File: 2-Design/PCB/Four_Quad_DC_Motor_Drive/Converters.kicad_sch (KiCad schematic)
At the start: 4 parts

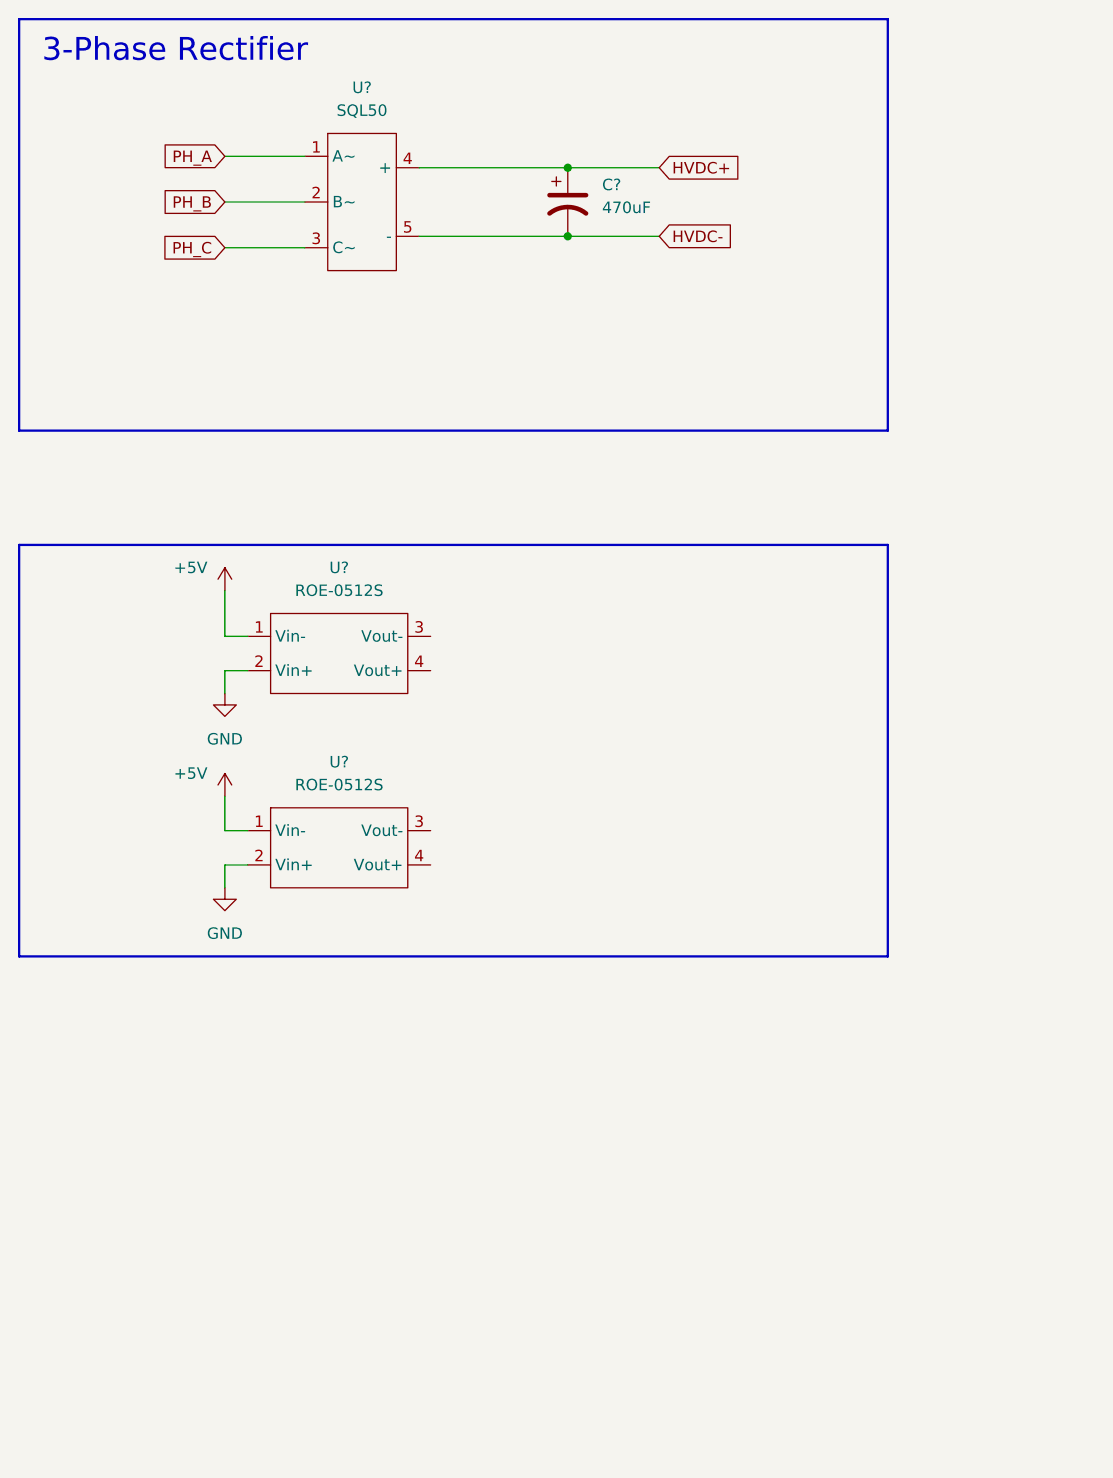
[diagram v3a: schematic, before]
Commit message: Added the gate driver schematics and converter schematics
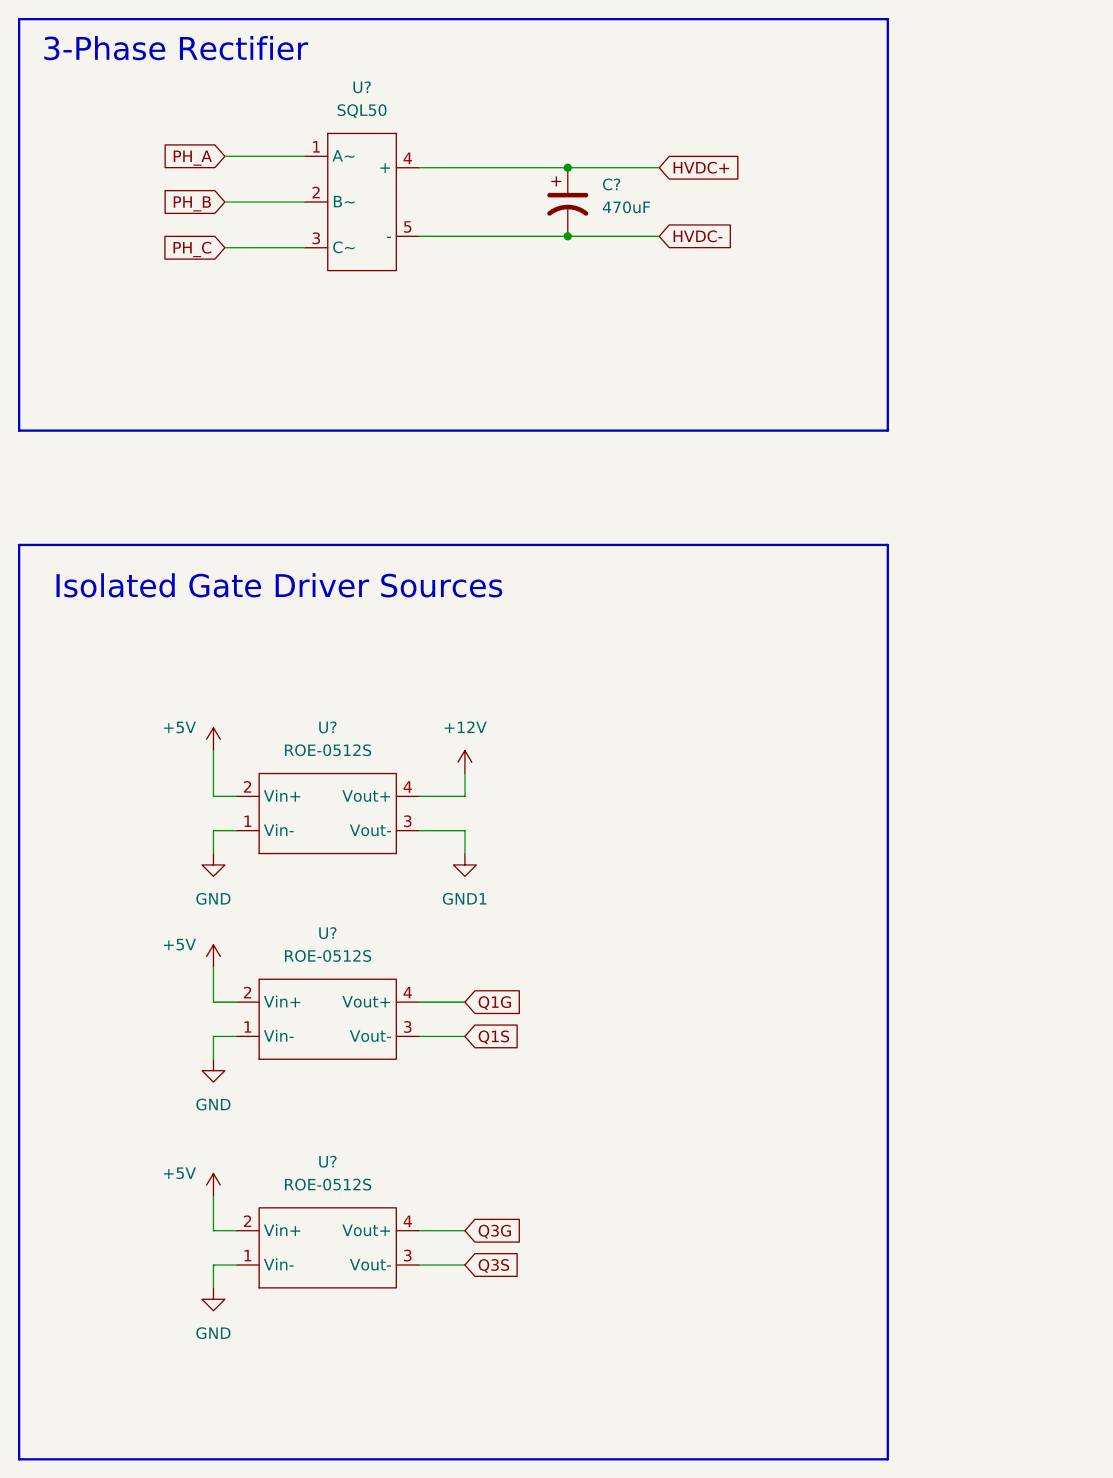
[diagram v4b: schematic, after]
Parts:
- added U?: ROE-0512S, symbol ee463_symbol_library:ROE-0512S
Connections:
- net +5V: now also U?.2 (Vin+), U?.2 (Vin+), U?.2 (Vin+); no longer U?.1 (Vin-), U?.1 (Vin-)
- net GND: now also U?.1 (Vin-), U?.1 (Vin-), U?.1 (Vin-); no longer U?.2 (Vin+), U?.2 (Vin+)
- net Q1S: now reaches U?.3 (Vout-)
- net Q1G: now reaches U?.4 (Vout+)
- net GND1: now reaches U?.3 (Vout-)
- net +12V: now reaches U?.4 (Vout+)
- new net Q3G: U?.4 (Vout+)
- new net Q3S: U?.3 (Vout-)
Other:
- note added: "Isolated Gate Driver Sources"
- moved on the sheet: U?

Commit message: Added the label and gate drive resistances
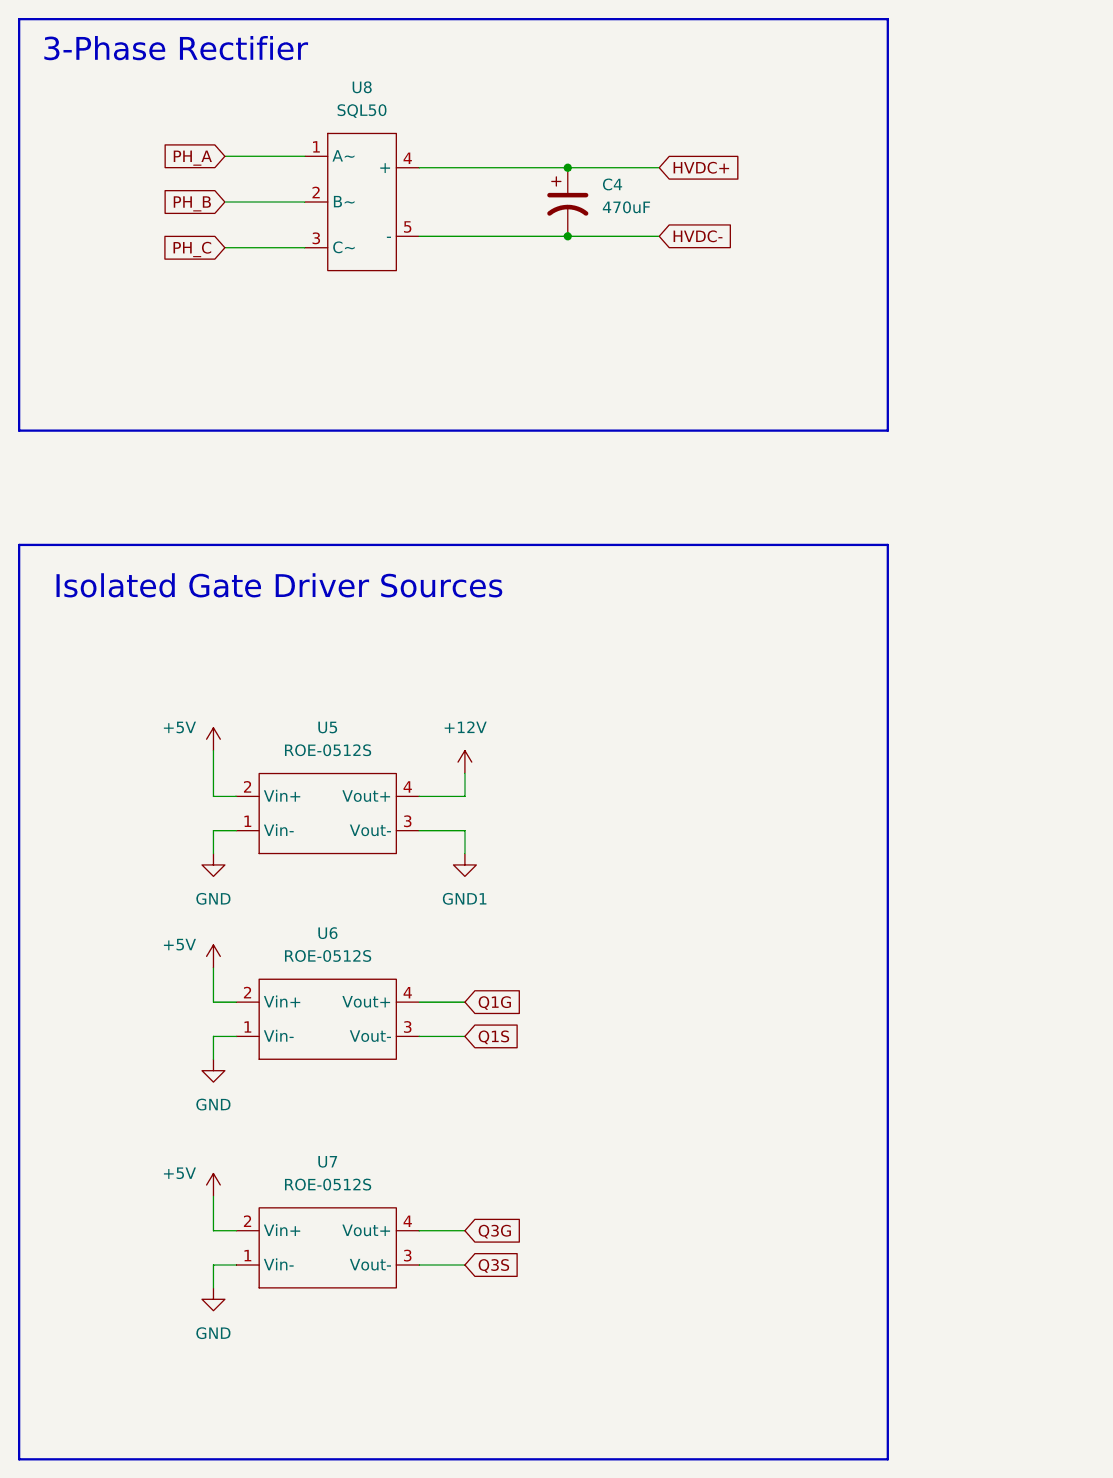
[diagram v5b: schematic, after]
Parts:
- gave numbers to parts that had none: 5
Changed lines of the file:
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@@
   (symbol (lib_id "power:+12V") (at 87.63 104.14 0) (unit 1)
     (in_bom yes) (on_board yes) (fields_autoplaced)
-    (property "Reference" "#PWR?" (id 0) (at 87.63 107.95 0)
+    (property "Reference" "#PWR018" (id 0) (at 87.63 107.95 0)
       (effects (font (size 1.27 1.27)) hide)
     )
@@
   (symbol (lib_id "power:GND") (at 59.69 161.29 0) (unit 1)
     (in_bom yes) (on_board yes) (fields_autoplaced)
-    (property "Reference" "#PWR?" (id 0) (at 59.69 167.64 0)
+    (property "Reference" "#PWR017" (id 0) (at 59.69 167.64 0)
       (effects (font (size 1.27 1.27)) hide)
     )
@@
   (symbol (lib_id "ee463_symbol_library:ROE-0512S") (at 72.39 132.08 0) (mirror x) (unit 1)
     (in_bom yes) (on_board yes) (fields_autoplaced)
-    (property "Reference" "U?" (id 0) (at 72.39 121.92 0))
+    (property "Reference" "U6" (id 0) (at 72.39 121.92 0))
     (property "Value" "ROE-0512S" (id 1) (at 72.39 124.46 0))
     (property "Footprint" "" (id 2) (at 72.39 132.08 0)
@@
   (symbol (lib_id "ee463_symbol_library:ROE-0512S") (at 72.39 109.22 0) (mirror x) (unit 1)
     (in_bom yes) (on_board yes) (fields_autoplaced)
-    (property "Reference" "U?" (id 0) (at 72.39 99.06 0))
+    (property "Reference" "U5" (id 0) (at 72.39 99.06 0))
     (property "Value" "ROE-0512S" (id 1) (at 72.39 101.6 0))
     (property "Footprint" "" (id 2) (at 72.39 109.22 0)
@@
   (symbol (lib_id "power:+5V") (at 59.69 101.6 0) (unit 1)
     (in_bom yes) (on_board yes)
-    (property "Reference" "#PWR?" (id 0) (at 59.69 105.41 0)
+    (property "Reference" "#PWR012" (id 0) (at 59.69 105.41 0)
       (effects (font (size 1.27 1.27)) hide)
     )
@@
   (symbol (lib_id "power:+5V") (at 59.69 151.13 0) (unit 1)
     (in_bom yes) (on_board yes)
-    (property "Reference" "#PWR?" (id 0) (at 59.69 154.94 0)
+    (property "Reference" "#PWR016" (id 0) (at 59.69 154.94 0)
       (effects (font (size 1.27 1.27)) hide)
     )
@@
   (symbol (lib_id "power:GND1") (at 87.63 113.03 0) (unit 1)
     (in_bom yes) (on_board yes) (fields_autoplaced)
-    (property "Reference" "#PWR?" (id 0) (at 87.63 119.38 0)
+    (property "Reference" "#PWR019" (id 0) (at 87.63 119.38 0)
       (effects (font (size 1.27 1.27)) hide)
     )
@@
   (symbol (lib_id "Device:C_Polarized_US") (at 99.06 40.64 0) (unit 1)
     (in_bom yes) (on_board yes) (fields_autoplaced)
-    (property "Reference" "C?" (id 0) (at 102.87 38.7349 0)
+    (property "Reference" "C4" (id 0) (at 102.87 38.7349 0)
       (effects (font (size 1.27 1.27)) (justify left))
     )
@@
   (symbol (lib_id "power:GND") (at 59.69 113.03 0) (unit 1)
     (in_bom yes) (on_board yes) (fields_autoplaced)
-    (property "Reference" "#PWR?" (id 0) (at 59.69 119.38 0)
+    (property "Reference" "#PWR013" (id 0) (at 59.69 119.38 0)
       (effects (font (size 1.27 1.27)) hide)
     )
@@
   (symbol (lib_id "ee463_symbol_library:SQL50") (at 76.2 40.64 0) (unit 1)
     (in_bom yes) (on_board yes) (fields_autoplaced)
-    (property "Reference" "U?" (id 0) (at 76.2 27.94 0))
+    (property "Reference" "U8" (id 0) (at 76.2 27.94 0))
     (property "Value" "SQL50" (id 1) (at 76.2 30.48 0))
     (property "Footprint" "" (id 2) (at 76.2 40.64 0)
@@
   (symbol (lib_id "power:GND") (at 59.69 135.89 0) (unit 1)
     (in_bom yes) (on_board yes) (fields_autoplaced)
-    (property "Reference" "#PWR?" (id 0) (at 59.69 142.24 0)
+    (property "Reference" "#PWR015" (id 0) (at 59.69 142.24 0)
       (effects (font (size 1.27 1.27)) hide)
     )
@@
   (symbol (lib_id "power:+5V") (at 59.69 125.73 0) (unit 1)
     (in_bom yes) (on_board yes)
-    (property "Reference" "#PWR?" (id 0) (at 59.69 129.54 0)
+    (property "Reference" "#PWR014" (id 0) (at 59.69 129.54 0)
       (effects (font (size 1.27 1.27)) hide)
     )
@@
   (symbol (lib_id "ee463_symbol_library:ROE-0512S") (at 72.39 157.48 0) (mirror x) (unit 1)
     (in_bom yes) (on_board yes) (fields_autoplaced)
-    (property "Reference" "U?" (id 0) (at 72.39 147.32 0))
+    (property "Reference" "U7" (id 0) (at 72.39 147.32 0))
     (property "Value" "ROE-0512S" (id 1) (at 72.39 149.86 0))
     (property "Footprint" "" (id 2) (at 72.39 157.48 0)

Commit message: Gate driver changed, plus other rearrangements on the schematics
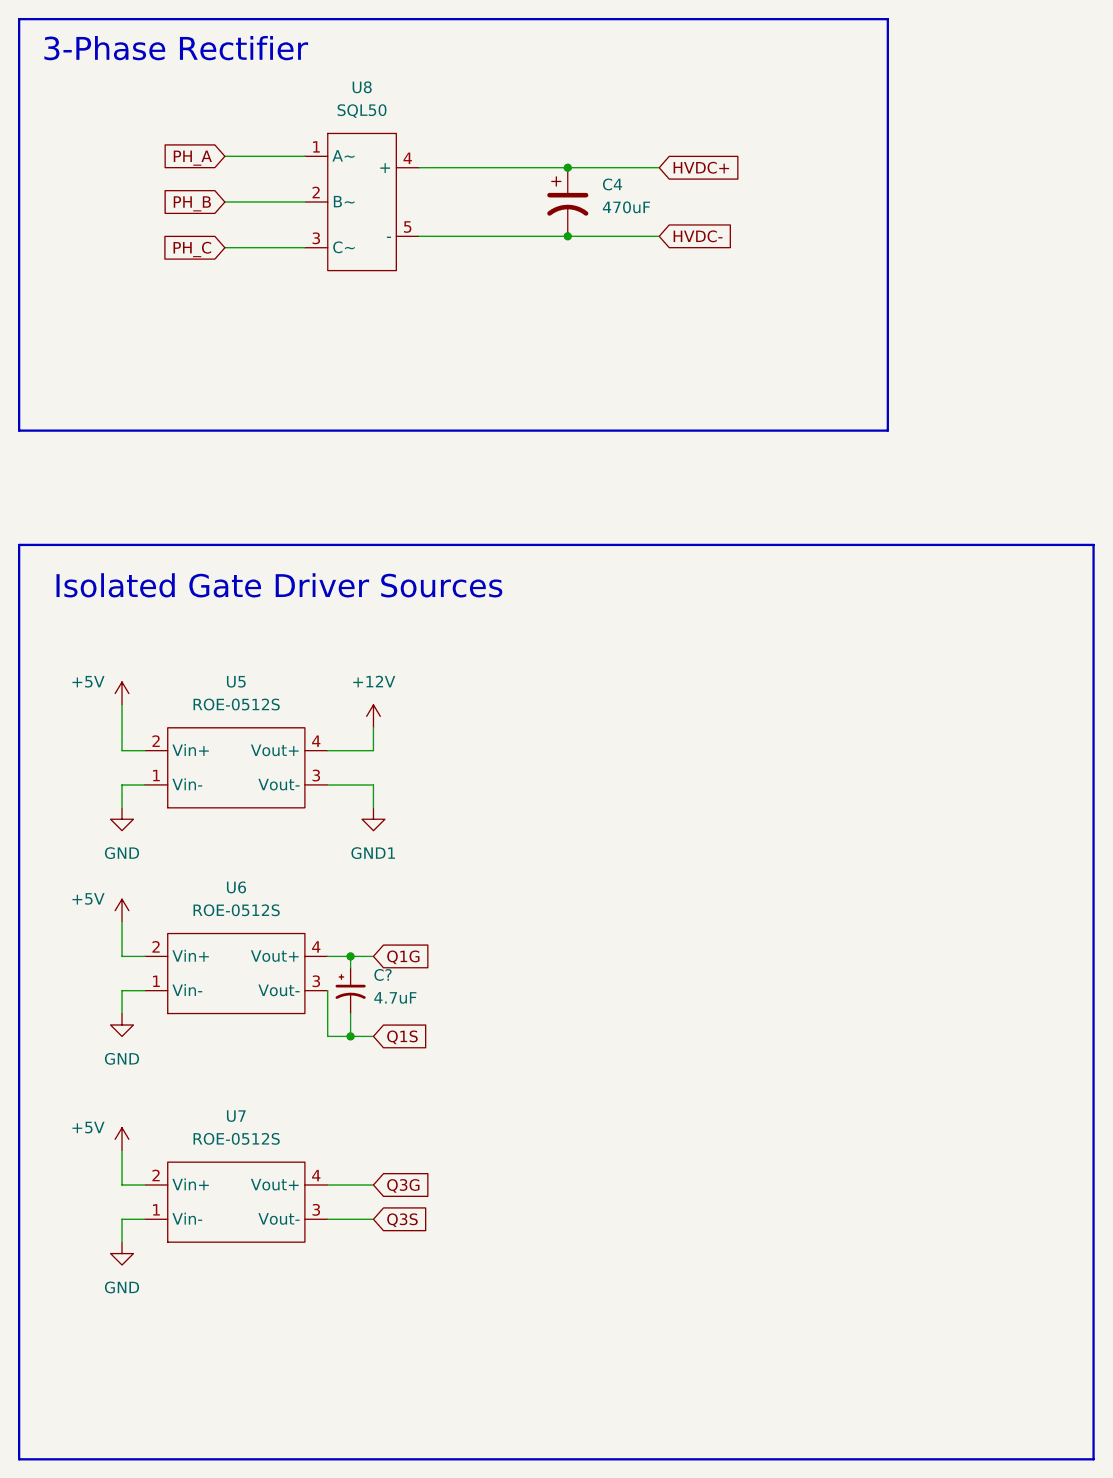
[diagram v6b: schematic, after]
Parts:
- added C?: 4.7uF, symbol Device:C_Polarized_Small_US
- U5, U6, U7: footprint (none) -> ee463_footprint_lib:ROE-0512S
- U8: footprint (none) -> ee463_footprint_lib:SQL50
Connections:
- net Q1G: now also C?.1
- net Q1S: now also C?.2
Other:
- moved on the sheet: U5, U6, U7

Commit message: Gate drivers finished, controller pins to be arranged
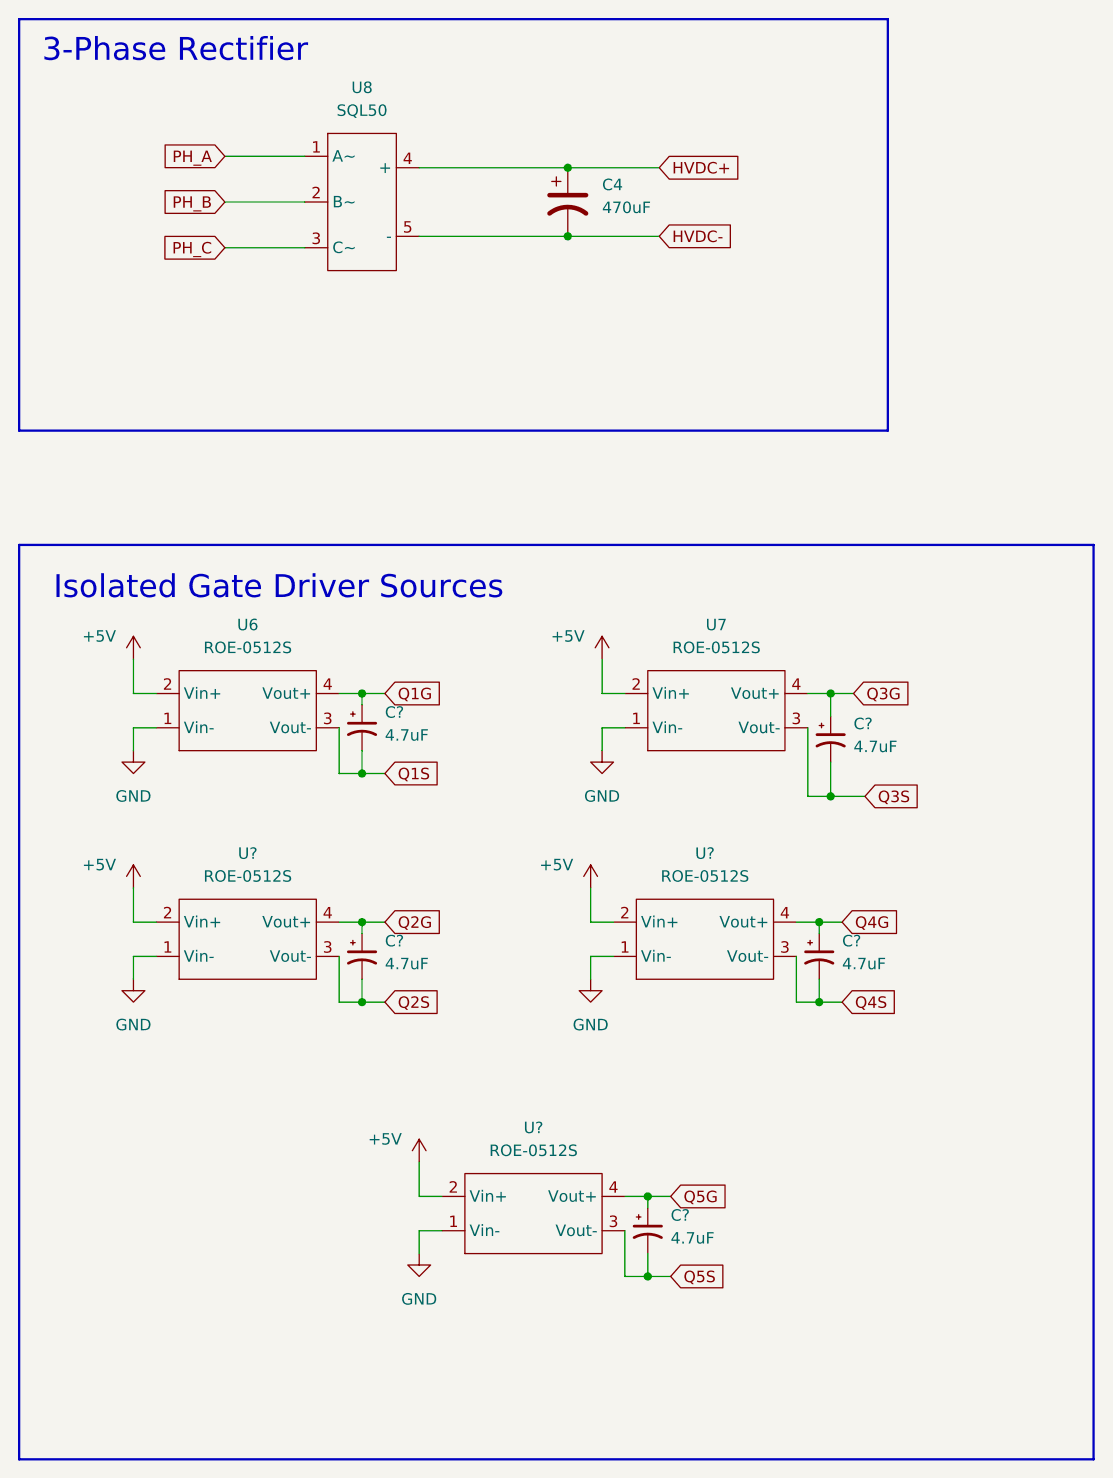
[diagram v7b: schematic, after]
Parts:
- removed U5: ROE-0512S, ee463_footprint_lib:ROE-0512S, symbol ee463_symbol_library:ROE-0512S
- added C? (x4): 4.7uF, symbol Device:C_Polarized_Small_US
- added U? (x3): ROE-0512S, ee463_footprint_lib:ROE-0512S, symbol ee463_symbol_library:ROE-0512S
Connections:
- net +5V: now also U?.2 (Vin+), U?.2 (Vin+), U?.2 (Vin+)
- net GND: now also U?.1 (Vin-), U?.1 (Vin-), U?.1 (Vin-)
- net Q3G: now also C?.1
- net Q3S: now also C?.2
- new net Q2G: C?.1, U?.4 (Vout+)
- new net Q2S: C?.2, U?.3 (Vout-)
- new net Q4G: C?.1, U?.4 (Vout+)
- new net Q4S: C?.2, U?.3 (Vout-)
- new net Q5G: C?.1, U?.4 (Vout+)
- new net Q5S: C?.2, U?.3 (Vout-)
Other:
- moved on the sheet: C?, U6, U7
